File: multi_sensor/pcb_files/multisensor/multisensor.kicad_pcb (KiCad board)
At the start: 2 copper layers, 48.3 x 45.7 mm, 16 parts, among them J1 Conn_01x04_Male, J2 POWER_SELECTOR, J3 Conn_01x04_Male, J4 Conn_01x05_Male

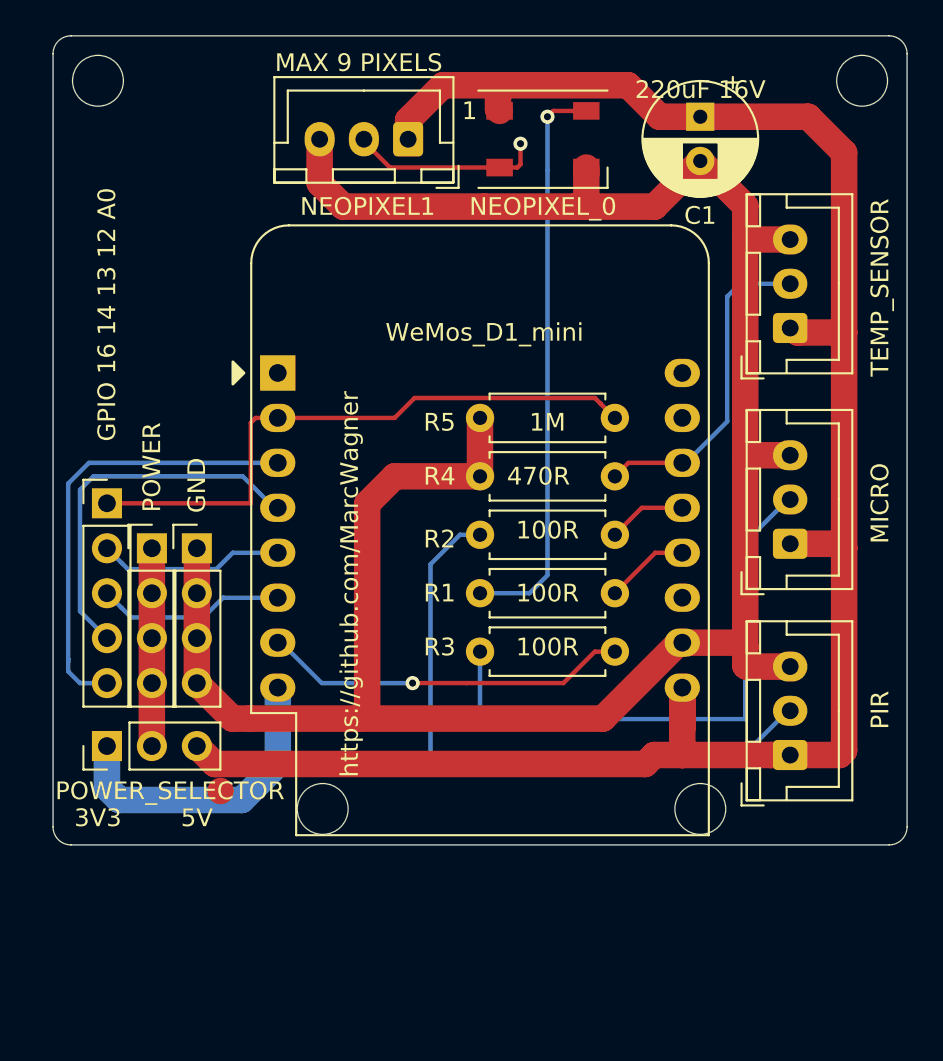
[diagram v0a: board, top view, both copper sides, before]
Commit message: updated pcb and logo
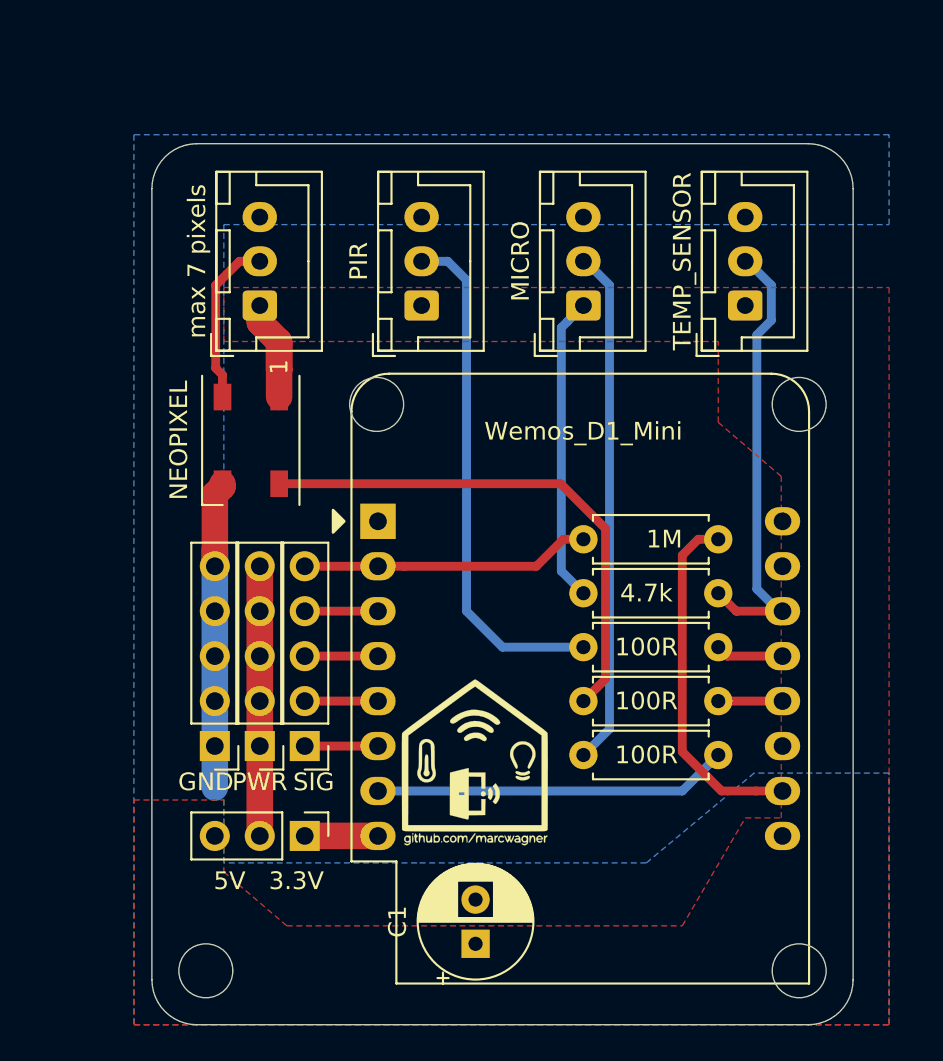
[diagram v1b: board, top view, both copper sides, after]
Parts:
- removed J1, J3: Conn_01x04_Male, Connector_PinHeader_2.54mm:PinHeader_1x04_P2.54mm_Vertical
- removed J2: POWER_SELECTOR, Connector_PinHeader_2.54mm:PinHeader_1x03_P2.54mm_Vertical
- removed J4: Conn_01x05_Male, Connector_PinHeader_2.54mm:PinHeader_1x05_P2.54mm_Vertical
- removed MICRO1, NEOPIXEL1, PIR1, TEMP_SENSOR1: Conn_01x03_Female, Connector_JST:JST_XH_B3B-XH-A_1x03_P2.50mm_Vertical
- removed NEOPIXEL_0: Inolux_IN-PI556FCH, LED_SMD:LED_WS2812B_PLCC4_5.0x5.0mm_P3.2mm
- removed Wemos_D1_Mini1: WeMos_D1_mini, Module:WEMOS_D1_mini_light
- added 5V   3.3V: Conn_01x04_Male, Connector_PinHeader_2.54mm:PinHeader_1x03_P2.54mm_Vertical, F.Cu at (54.9, 75.7)
- added G***: LOGO, sensor_logo:multisensor_logo, F.Cu at (64.5, 71.6)
- added G***: LOGO, sensor_logo:multisensor_logo, F.Cu at (72.1, 82.8)
- added G***: LOGO, sensor_logo:multisensor_logo, F.Cu at (100.6, 75.2)
- added GND: Conn_01x04_Male, Connector_PinHeader_2.54mm:PinHeader_1x05_P2.54mm_Vertical, F.Cu at (49.8, 70.6)
- added MICRO: Conn_01x03_Female, Connector_JST:JST_XH_B3B-XH-A_1x03_P2.50mm_Vertical, F.Cu at (70.6, 45.7)
- added NEOPIXEL: Inolux_IN-PI556FCH, LED_SMD:LED_WS2812B_PLCC4_5.0x5.0mm_P3.2mm, F.Cu at (51.8, 53.3)
- added PIR: Conn_01x03_Female, Connector_JST:JST_XH_B3B-XH-A_1x03_P2.50mm_Vertical, F.Cu at (61.5, 45.7)
- added PWR: Conn_01x04_Male, Connector_PinHeader_2.54mm:PinHeader_1x05_P2.54mm_Vertical, F.Cu at (52.3, 70.6)
- added SIG: Conn_01x05_Male, Connector_PinHeader_2.54mm:PinHeader_1x05_P2.54mm_Vertical, F.Cu at (54.9, 70.6)
- added TEMP_SENSOR: Conn_01x03_Female, Connector_JST:JST_XH_B3B-XH-A_1x03_P2.50mm_Vertical, F.Cu at (79.8, 45.7)
- added Wemos_D1_Mini: WeMos_D1_mini, Module:WEMOS_D1_mini_light, F.Cu at (59.0, 57.9)
- added max 7 pixels: Conn_01x03_Female, Connector_JST:JST_XH_B3B-XH-A_1x03_P2.50mm_Vertical, F.Cu at (52.3, 45.7)
- R4: value 470R -> 4.7k
- moved C1 48.4 mm to (64.5, 81.8), turned to 90 degrees
- moved R5 15.1 mm to (78.2, 58.9), turned to 180 degrees
- moved R2 8.63 mm to (70.6, 65.0)
- moved R1 8.44 mm to (70.6, 68.1)
- moved R3 8.26 mm to (70.6, 71.1)
- moved R4 6.84 mm to (70.6, 62.0), turned to 0 degrees
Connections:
- R1 pad 2: /NEOPIXEL -> /NEOPIXEL_S
- R2 pad 2: /PIR -> /PIR_S
- R3 pad 2: /MICRO -> /MICRO_S
- R4 pad 1: /TEMP_SENSOR -> +5V
- R4 pad 2: GND -> /TEMP_SENSOR_S
- R5 pad 2: /ANALOG -> /ANALOG_S
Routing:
- net GND: track 166.6 -> 38.7 mm
- net +5V: track 128.7 -> 24.4 mm
- net /ANALOG: track 34.3 -> 0.00 mm
- net /GPIO16: track 25.6 -> 0.00 mm
- net /TEMP_SENSOR_S: track 0.00 -> 25.6 mm
- net /GPIO14: track 21.2 -> 0.00 mm
- net /MICRO: track 20.7 -> 0.00 mm, vias 1 -> 0
- net /MICRO_S: track 0.00 -> 20.1 mm
- net /TEMP_SENSOR: track 18.5 -> 0.00 mm
- net /ANALOG_S: track 0.00 -> 16.4 mm
- net +3V3: track 17.5 -> 4.14 mm
- net /GPIO13: track 10.9 -> 0.00 mm
- net /GPIO12: track 10.7 -> 0.00 mm
- net Net-(PIR1-Pad2): track 36.1 -> 29.1 mm
- net /NEOPIXEL: track 4.76 -> 0.00 mm
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- added copper zone on F.Cu, net +5V
- added copper zone on B.Cu, net GND
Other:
- board size 48.3 x 45.7 mm -> 39.6 x 49.8 mm
- net class Default: trace_width 0.25 -> 0.5
- board text added: "Multisensor v2 Marc Wagner"
- board text removed: "3V3"
- board text removed: "5V"
- board text removed: "GND"
- board text removed: "GPIO 16 14 13 12 A0"
- board text removed: "MAX 9 PIXELS"
- board text removed: "MICRO"
- board text removed: "PIR"
- board text removed: "POWER"
- board text removed: "TEMP_SENSOR"
- board text removed: "https://github.com/MarcWagner"

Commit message: updating pcb schematics
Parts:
- NEOPIXEL1: renamed from max 7 pixels
- POWER_SELECT1: renamed from 5V   3.3V
- moved R1 7.62 mm to (78.2, 68.1), turned to 180 degrees
- moved R3 7.62 mm to (78.2, 71.1), turned to 180 degrees
- renumbered GND to GND1, MICRO to MICRO1, NEOPIXEL to NEOPIXEL_0, PIR to PIR1, PWR to POWER1, SIG to SIGNAL1, TEMP_SENSOR to TEMP_SENSOR1, Wemos_D1_Mini to Wemos_D1_Mini1
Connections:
- SIGNAL1 pad 1: /GPIO13_S -> /GPIO15_S
- SIGNAL1 pad 2: /GPIO12_S -> /GPIO0_S
- Wemos_D1_Mini1 pad 12: /NEOPIXEL_S -> /GPIO0_S
- Wemos_D1_Mini1 pad 5: /GPIO12_S -> /NEOPIXEL_S
- Wemos_D1_Mini1 pad 6: /GPIO13_S -> /MICRO_S
- Wemos_D1_Mini1 pad 7: /MICRO_S -> /GPIO15_S
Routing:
- net /GPIO0_S: track 0.00 -> 34.8 mm
- net Net-(NEOPIXEL_0-Pad4): track 29.8 -> 40.1 mm
- net /MICRO_S: track 20.1 -> 12.0 mm
- net /NEOPIXEL_S: track 3.63 -> 11.6 mm
- net /GPIO15_S: track 0.00 -> 5.98 mm
- net /GPIO13_S: track 4.14 -> 0.00 mm
- net /GPIO12_S: track 4.14 -> 0.00 mm
- net Net-(MICRO1-Pad2): track 29.2 -> 31.1 mm
